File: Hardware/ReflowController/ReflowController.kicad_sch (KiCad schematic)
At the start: 11 parts, among them J101 2060-1452, J102 2060-1452, J103 2060-1453, J104 2060-1452, J105 2060-1452, J106 2060-1452, J107 2060-1452, J108 2060-1452, J109 2060-1452, J110 2060-1452, J111 2060-1452

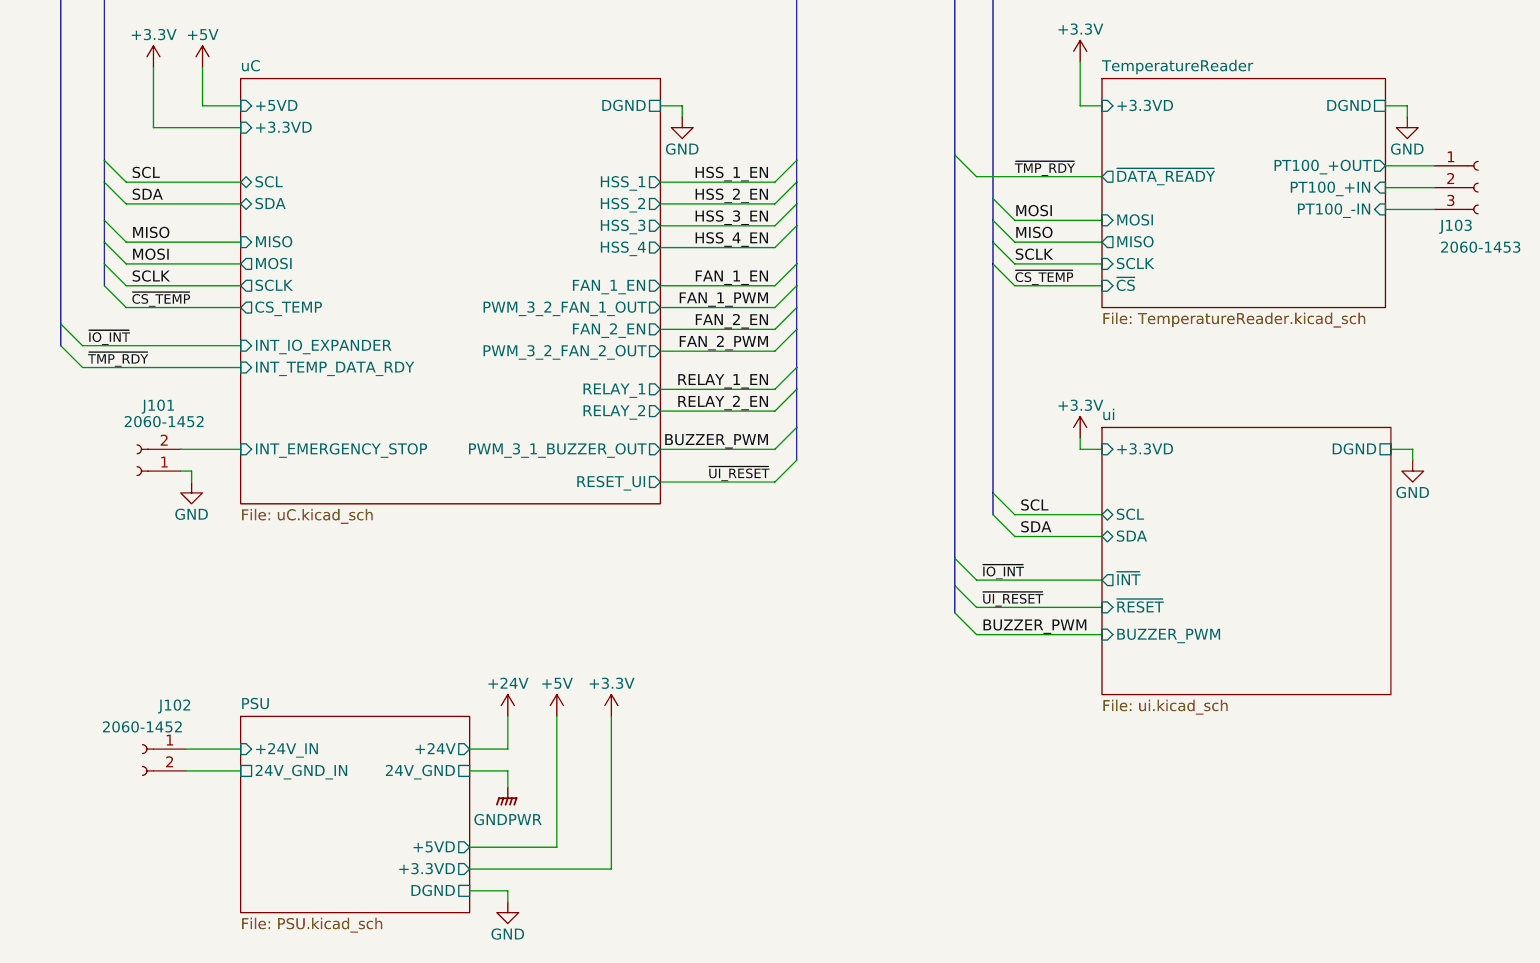
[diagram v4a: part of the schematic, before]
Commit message: Made some progress on the PCB desgin for now only the main blocks are complete, thw pin connection of the mCU should be organised and Net-ties are making life much harder as you cant put them on the middle layers
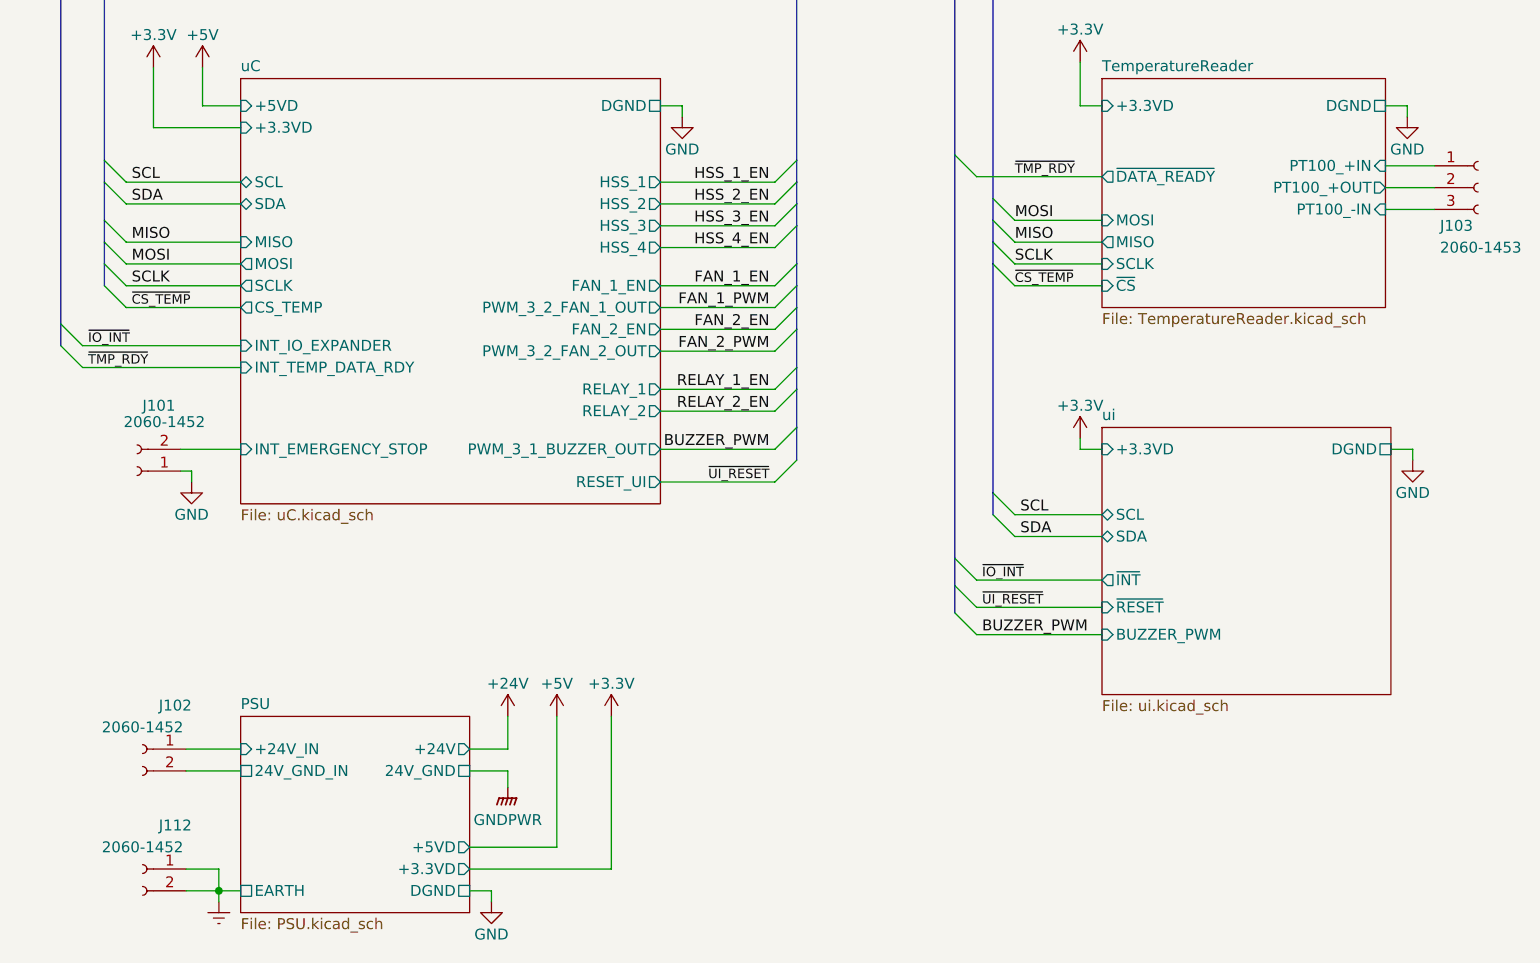
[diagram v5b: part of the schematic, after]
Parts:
- added J112: 2060-1452, 810_connectors_clable_to_Board:wago_2060-1452, symbol Connector:Conn_01x02_Socket
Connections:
- net TemperatureReader/PT100_+IN: now also J103.1 (Pin_1); no longer J103.2 (Pin_2)
- net TemperatureReader/PT100_+OUT: now also J103.2 (Pin_2); no longer J103.1 (Pin_1)
- new net Earth: J112.1 (Pin_1), J112.2 (Pin_2)
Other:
- sheet PSU ports: added EARTH; removed none
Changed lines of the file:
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@@
   (junction (at 17.78 21.59) (diameter 0) (color 0 0 0 0)
   )
+  (junction (at 36.195 131.445) (diameter 0) (color 0 0 0 0)
+  )
   (junction (at 22.86 17.78) (diameter 0) (color 0 0 0 0)
   )
@@
     (stroke (width 0) (type default))
   )
+  (wire (pts (xy 36.195 128.905) (xy 36.195 131.445))
+    (stroke (width 0) (type default))
+  )
   (bus (pts (xy 22.86 53.34) (xy 22.86 55.88))
     (stroke (width 0) (type default))
   )
+  (wire (pts (xy 32.385 128.905) (xy 36.195 128.905))
+    (stroke (width 0) (type default))
+  )
   (bus (pts (xy 126.365 50.8) (xy 126.365 53.34))
     (stroke (width 0) (type default))
@@
     (stroke (width 0) (type default))
   )
+  (wire (pts (xy 32.385 131.445) (xy 36.195 131.445))
+    (stroke (width 0) (type default))
+  )
   (bus (pts (xy 126.365 55.88) (xy 126.365 58.42))
     (stroke (width 0) (type default))
@@
     (stroke (width 0) (type default))
   )
-  (wire (pts (xy 69.85 131.445) (xy 69.85 132.715))
-    (stroke (width 0) (type default))
-  )
   (wire (pts (xy 212.09 66.675) (xy 228.6 66.675))
     (stroke (width 0) (type default))
@@
     (stroke (width 0) (type default))
   )
-  (wire (pts (xy 65.405 131.445) (xy 69.85 131.445))
-    (stroke (width 0) (type default))
-  )
   (wire (pts (xy 87.63 56.515) (xy 100.965 56.515))
     (stroke (width 0) (type default))
@@
     (stroke (width 0) (type default))
   )
+  (wire (pts (xy 36.195 131.445) (xy 36.195 132.715))
+    (stroke (width 0) (type default))
+  )
   (bus (pts (xy 209.55 70.485) (xy 209.55 78.105))
     (stroke (width 0) (type default))
@@
     (stroke (width 0) (type default))
   )
+  (wire (pts (xy 65.405 131.445) (xy 67.945 131.445))
+    (stroke (width 0) (type default))
+  )
   (wire (pts (xy 261.62 40.005) (xy 266.7 40.005))
     (stroke (width 0) (type default))
@@
     (stroke (width 0) (type default))
   )
+  (wire (pts (xy 36.195 131.445) (xy 38.735 131.445))
+    (stroke (width 0) (type default))
+  )
   (bus (pts (xy 22.86 58.42) (xy 22.86 60.96))
     (stroke (width 0) (type default))
@@
   )
   (bus (pts (xy 17.78 21.59) (xy 17.78 65.405))
+    (stroke (width 0) (type default))
+  )
+  (wire (pts (xy 67.945 131.445) (xy 67.945 132.715))
     (stroke (width 0) (type default))
   )
@@
         (path "/2394cc2a-b9b0-4c0b-be11-1fc6085b0d5c"
           (reference "#PWR0115") (unit 1)
+        )
+      )
+    )
+  )
+  (symbol (lib_id "power:Earth") (at 36.195 132.715 0) (unit 1)
+    (in_bom yes) (on_board yes) (dnp no) (fields_autoplaced)
+    (property "Reference" "#PWR0121" (at 36.195 139.065 0)
+      (effects (font (size 1.27 1.27)) hide)
+    )
+    (property "Value" "Earth" (at 36.195 136.525 0)
+      (effects (font (size 1.27 1.27)) hide)
+    )
+    (property "Footprint" "" (at 36.195 132.715 0)
+      (effects (font (size 1.27 1.27)) hide)
+    )
+    (property "Datasheet" "~" (at 36.195 132.715 0)
+      (effects (font (size 1.27 1.27)) hide)
+    )
+    (pin "1")
+    (instances
+      (project "ReflowController"
+        (path "/2394cc2a-b9b0-4c0b-be11-1fc6085b0d5c"
+          (reference "#PWR0121") (unit 1)
         )
       )
@@
     )
   )
-  (symbol (lib_id "power:GND") (at 69.85 132.715 0) (unit 1)
+  (symbol (lib_id "power:GND") (at 67.945 132.715 0) (unit 1)
     (in_bom yes) (on_board yes) (dnp no)
-    (property "Reference" "#PWR0106" (at 69.85 139.065 0)
-      (effects (font (size 1.27 1.27)) hide)
-    )
-    (property "Value" "GND" (at 69.85 136.525 0)
-      (effects (font (size 1.27 1.27)))
-    )
-    (property "Footprint" "" (at 69.85 132.715 0)
-      (effects (font (size 1.27 1.27)) hide)
-    )
-    (property "Datasheet" "" (at 69.85 132.715 0)
+    (property "Reference" "#PWR0106" (at 67.945 139.065 0)
+      (effects (font (size 1.27 1.27)) hide)
+    )
+    (property "Value" "GND" (at 67.945 136.525 0)
+      (effects (font (size 1.27 1.27)))
+    )
+    (property "Footprint" "" (at 67.945 132.715 0)
+      (effects (font (size 1.27 1.27)) hide)
+    )
+    (property "Datasheet" "" (at 67.945 132.715 0)
       (effects (font (size 1.27 1.27)) hide)
     )
@@
         (path "/2394cc2a-b9b0-4c0b-be11-1fc6085b0d5c"
           (reference "J106") (unit 1)
+        )
+      )
+    )
+  )
+  (symbol (lib_id "Connector:Conn_01x02_Socket") (at 27.305 128.905 0) (mirror y) (unit 1)
+    (in_bom yes) (on_board yes) (dnp no)
+    (property "Reference" "J112" (at 31.115 123.825 0)
+      (effects (font (size 1.27 1.27)))
+    )
+    (property "Value" "2060-1452" (at 27.305 126.365 0)
+      (effects (font (size 1.27 1.27)))
+    )
+    (property "Footprint" "810_connectors_clable_to_Board:wago_2060-1452" (at 27.305 128.905 0)
+      (effects (font (size 1.27 1.27)) hide)
+    )
+    (property "Datasheet" "~" (at 27.305 128.905 0)
+      (effects (font (size 1.27 1.27)) hide)
+    )
+    (property "man" "wago" (at 27.305 128.905 0)
+      (effects (font (size 1.27 1.27)) hide)
+    )
+    (property "man_no" "2060-1452" (at 27.305 128.905 0)
+      (effects (font (size 1.27 1.27)) hide)
+    )
+    (property "disti" "digikey" (at 27.305 128.905 0)
+      (effects (font (size 1.27 1.27)) hide)
+    )
+    (property "disti_no" "2946-2060-1452/998-404TR-ND" (at 27.305 128.905 0)
+      (effects (font (size 1.27 1.27)) hide)
+    )
+    (pin "1")
+    (pin "2")
+    (instances
+      (project "ReflowController"
+        (path "/2394cc2a-b9b0-4c0b-be11-1fc6085b0d5c"
+          (reference "J112") (unit 1)
         )
       )
@@
       (effects (font (size 1.27 1.27)) (justify right))
     )
-    (pin "PT100_+IN" input (at 172.085 49.53 0)
-      (effects (font (size 1.27 1.27)) (justify right))
-    )
-    (pin "PT100_+OUT" output (at 172.085 46.99 0)
+    (pin "PT100_+IN" input (at 172.085 46.99 0)
+      (effects (font (size 1.27 1.27)) (justify right))
+    )
+    (pin "PT100_+OUT" output (at 172.085 49.53 0)
       (effects (font (size 1.27 1.27)) (justify right))
     )
@@
       (effects (font (size 1.27 1.27)) (justify left))
     )
+    (pin "EARTH" passive (at 38.735 131.445 180)
+      (effects (font (size 1.27 1.27)) (justify left))
+    )

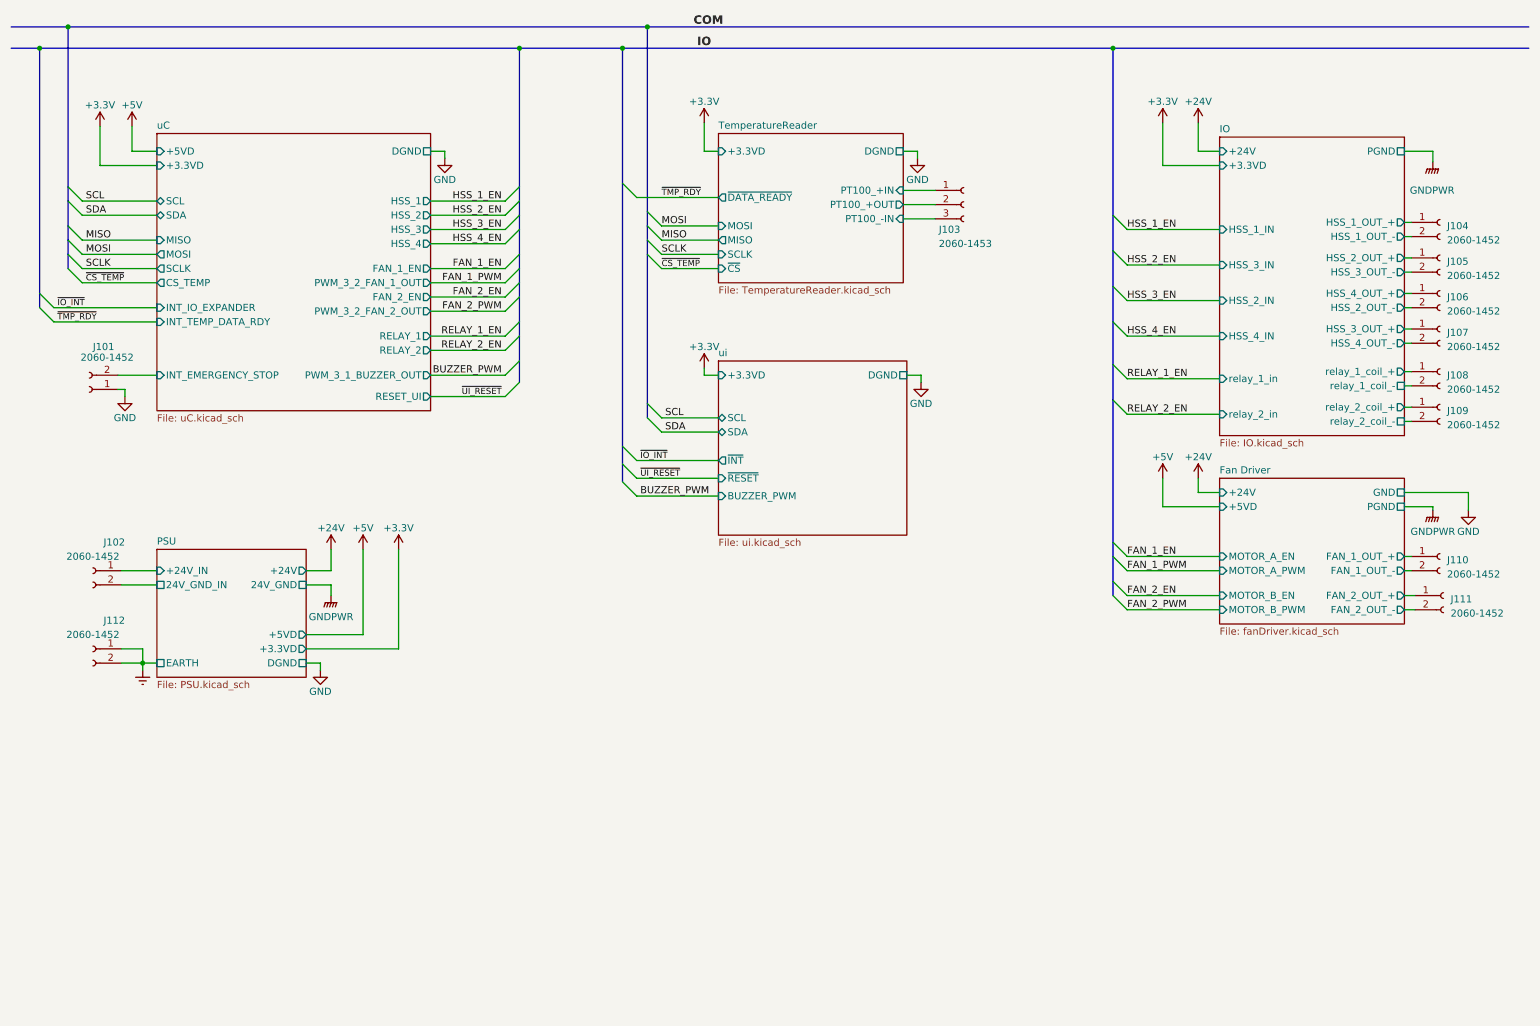
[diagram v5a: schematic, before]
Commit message: Advancing on the pcb removed netties from MCU
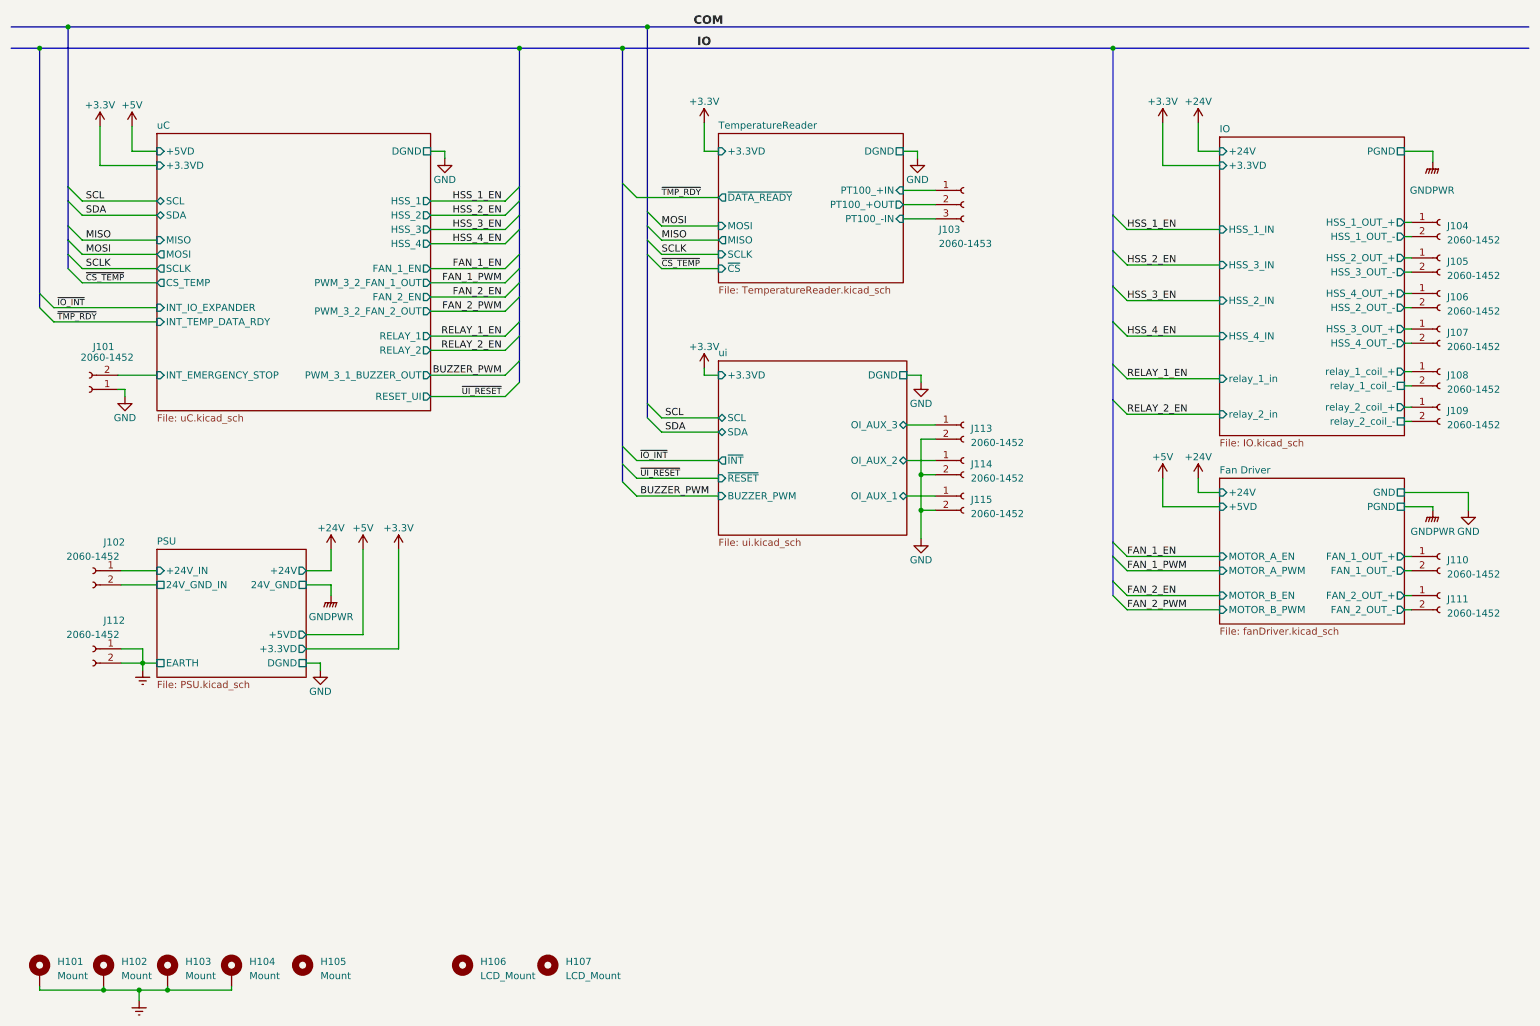
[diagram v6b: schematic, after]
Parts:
- added H101, H102, H103, H104: Mount, MountingHole:MountingHole_3.2mm_M3_Pad_Via, symbol Mechanical:MountingHole_Pad
- added H105: Mount, MountingHole:MountingHole_3.2mm_M3, symbol Mechanical:MountingHole
- added H106, H107: LCD_Mount, MountingHole:MountingHole_2.2mm_M2_ISO7380, symbol Mechanical:MountingHole
- added J113, J114, J115: 2060-1452, 810_connectors_clable_to_Board:wago_2060-1452, symbol Connector:Conn_01x02_Socket
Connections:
- net Earth: now also H101.1, H102.1, H103.1, H104.1
- net GND: now also J113.2 (Pin_2), J114.2 (Pin_2), J115.2 (Pin_2)
- new net ui/OI_AUX_1: J115.1 (Pin_1)
- new net ui/OI_AUX_2: J114.1 (Pin_1)
- new net ui/OI_AUX_3: J113.1 (Pin_1)
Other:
- sheet ui ports: added OI_AUX_1, OI_AUX_2, OI_AUX_3; removed none
- moved on the sheet: J111
